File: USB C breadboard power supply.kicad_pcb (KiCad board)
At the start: 4 copper layers, 56.5 x 37.8 mm, 43 parts, among them J1 Conn_02x02_Counter_Clockwise, J2 Conn_02x02_Counter_Clockwise, Q1 IRF9358TRPBF, SW1 SS-10-15SP-LE, U1 CYPD3177-24LQXQT, U2 AP63203WU

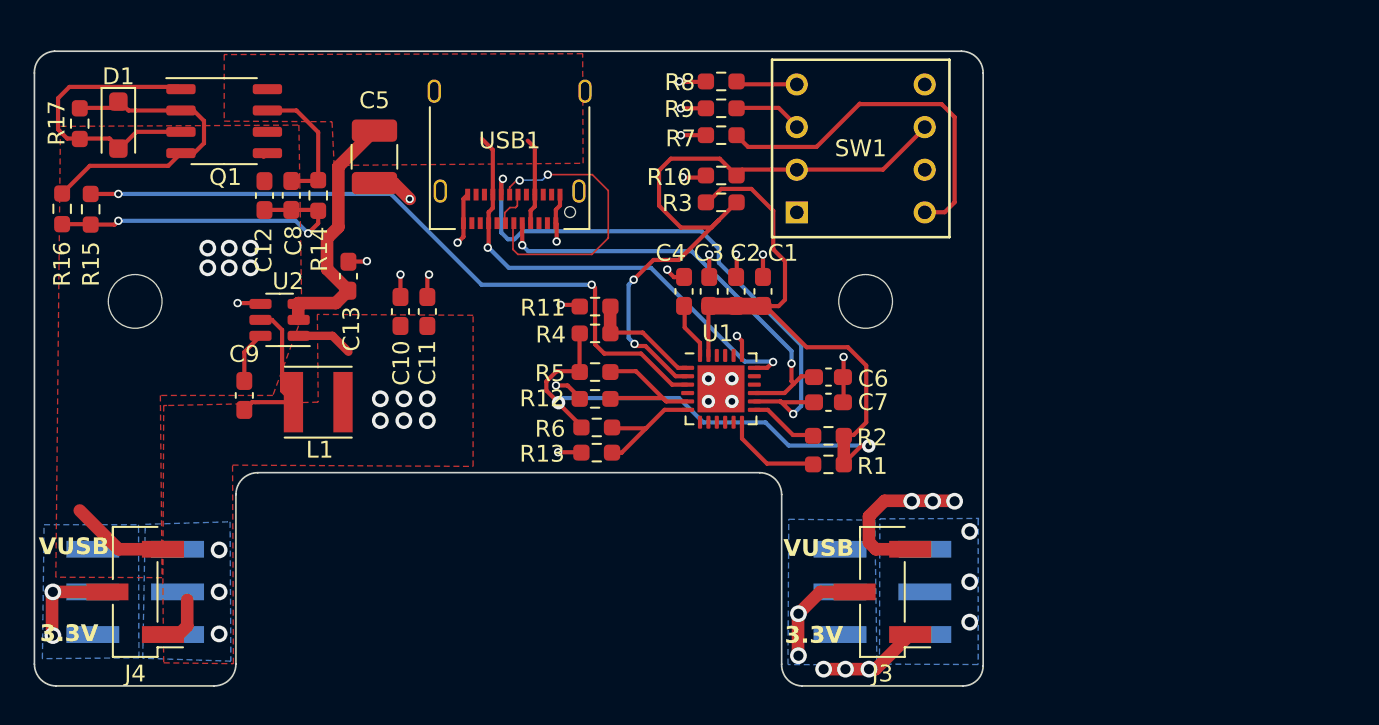
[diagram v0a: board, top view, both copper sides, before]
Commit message: Updated PCB layout
Reset the layout grid to use 1mm spacing. Changed board outline size. Adjusted copper fill zones and moved them to different layers. Added logo and moved some silkscreen objects.
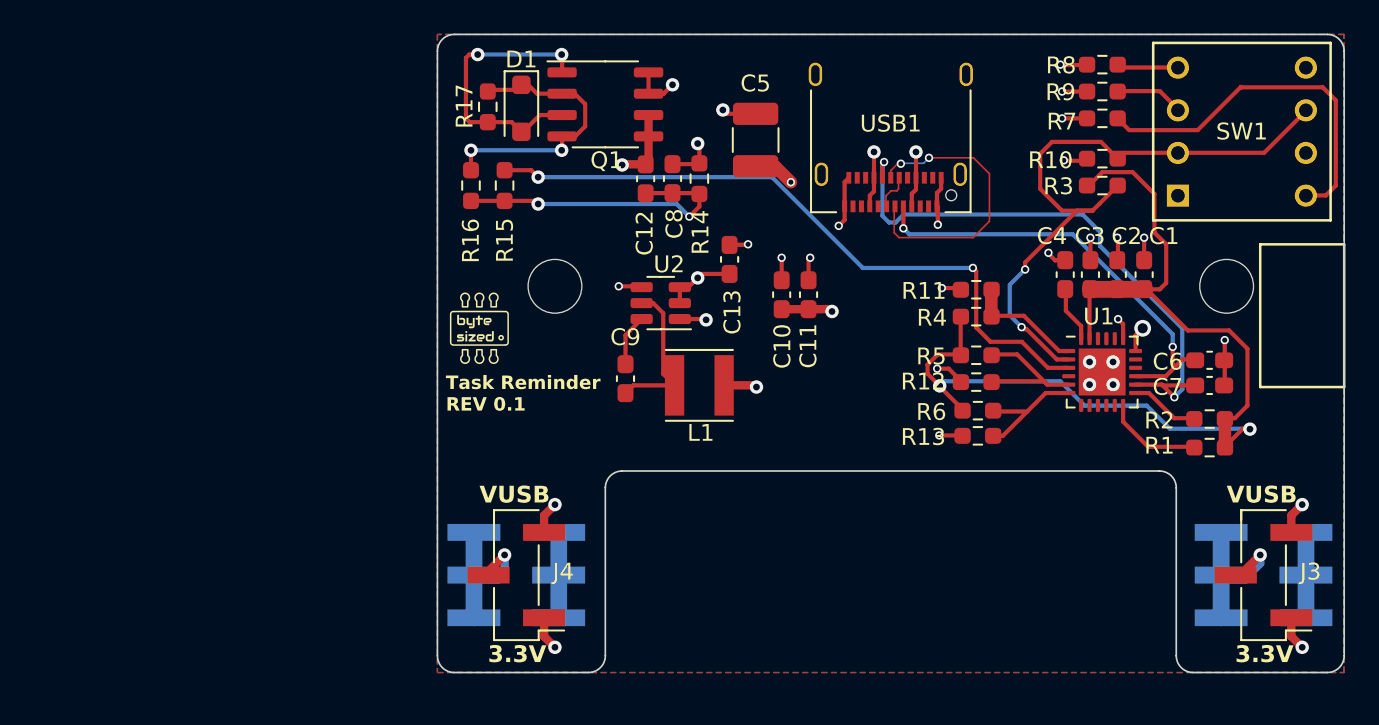
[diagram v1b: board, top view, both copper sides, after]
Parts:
- removed H1: MountingHole, MountingHole:MountingHole_3.2mm_M3
- added ?: , , F.Cu at (147.0, 115.0)
- added G***: LOGO, New Logo:byteSizedEngineeringLogo-5mm, F.Cu at (102.5, 117.5)
- moved H2 25.0 mm to (107.0, 115.0)
- moved R15 24.7 mm to (104.0, 109.0)
- moved R16 24.4 mm to (102.0, 109.0)
- moved R17 24.3 mm to (103.0, 104.3)
- moved D1 24.0 mm to (105.0, 104.4)
- moved C2 22.7 mm to (140.5, 114.3)
- moved C6 22.7 mm to (146.0, 119.4)
- moved C7 22.7 mm to (146.0, 120.9)
- moved R1 22.7 mm to (146.0, 124.6)
- moved R2 22.7 mm to (146.0, 122.9)
- moved C1 22.7 mm to (142.1, 114.3)
- moved C10 22.7 mm to (120.5, 115.5)
- moved C12 22.7 mm to (112.4, 108.6)
- moved C13 22.7 mm to (117.4, 113.4)
- moved C5 22.7 mm to (119.0, 106.3)
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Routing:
- net VBUS: track 56.5 -> 20.3 mm, vias 2 -> 7
- net GND: track 33.0 -> 43.2 mm, vias 30 -> 24
- net /DC_OUTPUT: track 15.9 -> 8.28 mm, vias 9 -> 3
- net /RAIL_1: track 6.37 -> 10.1 mm, vias 2 -> 1
- net /RAIL_2: track 5.89 -> 9.58 mm, vias 2 -> 1
- net Net-(D1-K): track 19.1 -> 16.8 mm, vias 0 -> 2
- net /3V3_OUT: track 12.5 -> 10.7 mm, vias 9 -> 5
- net /VBUS_FET_EN: track 42.2 -> 40.4 mm
- net Net-(C12-Pad1): track 19.9 -> 18.2 mm
- net /VBUS_MAX: track 40.2 -> 39.1 mm
- net Net-(D1-A): track 17.7 -> 16.9 mm, vias 0 -> 2
- added copper zone on In1.Cu, net /DC_OUTPUT
- added copper zone on F.Cu, net GND
- added copper zone on In1.Cu, net VBUS
- removed copper zone on F.Cu, net /3V3_OUT
- removed copper zone on F.Cu, net /DC_OUTPUT
- removed copper zone on In2.Cu, net /DC_OUTPUT
- removed copper zone on B.Cu, net /RAIL_1
- removed copper zone on B.Cu, net /RAIL_2
- removed copper zone on In1.Cu, net GND
- removed copper zone on F.Cu, net VBUS
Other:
- board size 56.5 x 37.8 mm -> 54 x 38 mm
- board text added: "${TITLE} REV ${REVISION}"
